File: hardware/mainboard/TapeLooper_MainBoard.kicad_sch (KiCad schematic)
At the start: 4 parts, among them J101 Micro_SD_Card, U101 DAISY_SEED

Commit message: hardware: resave files with KiCad v7.0.4
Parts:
- gave numbers to parts that had none: 2

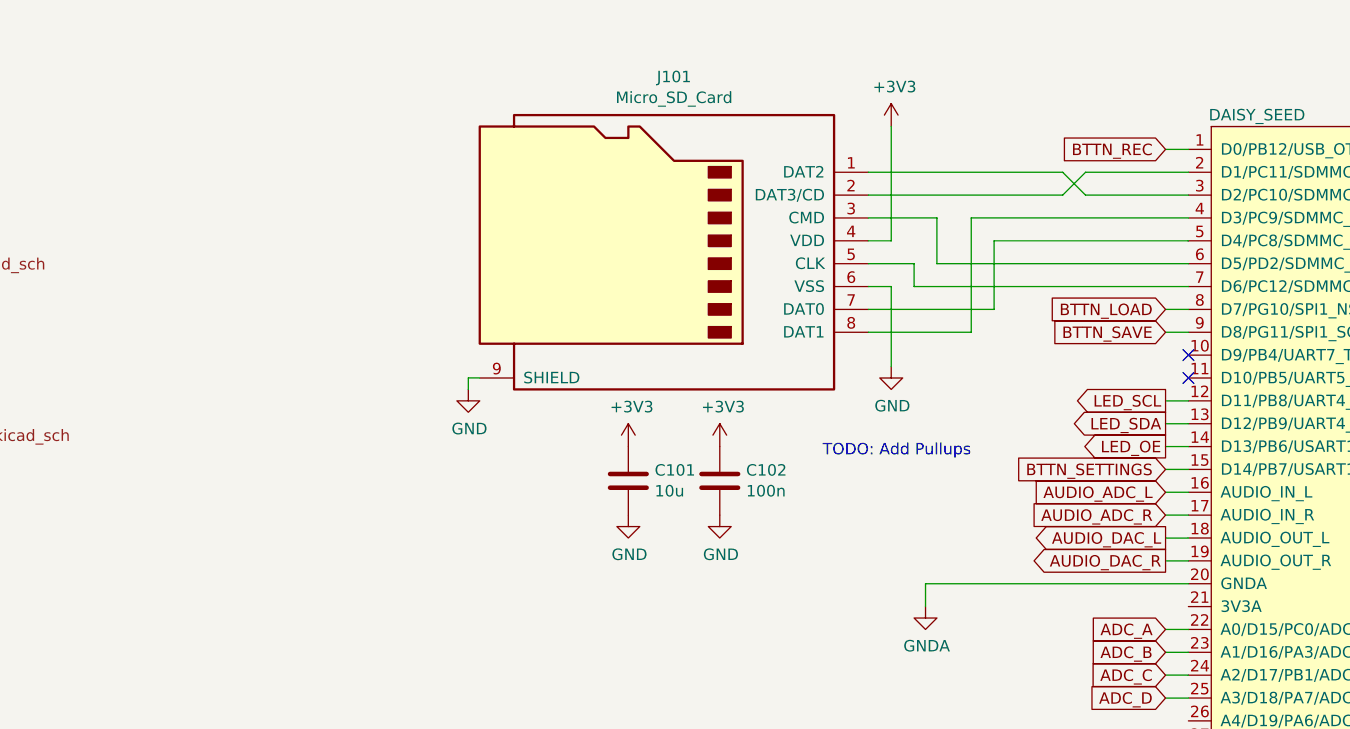
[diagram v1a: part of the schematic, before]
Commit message: hardware: add missing SD card pullups
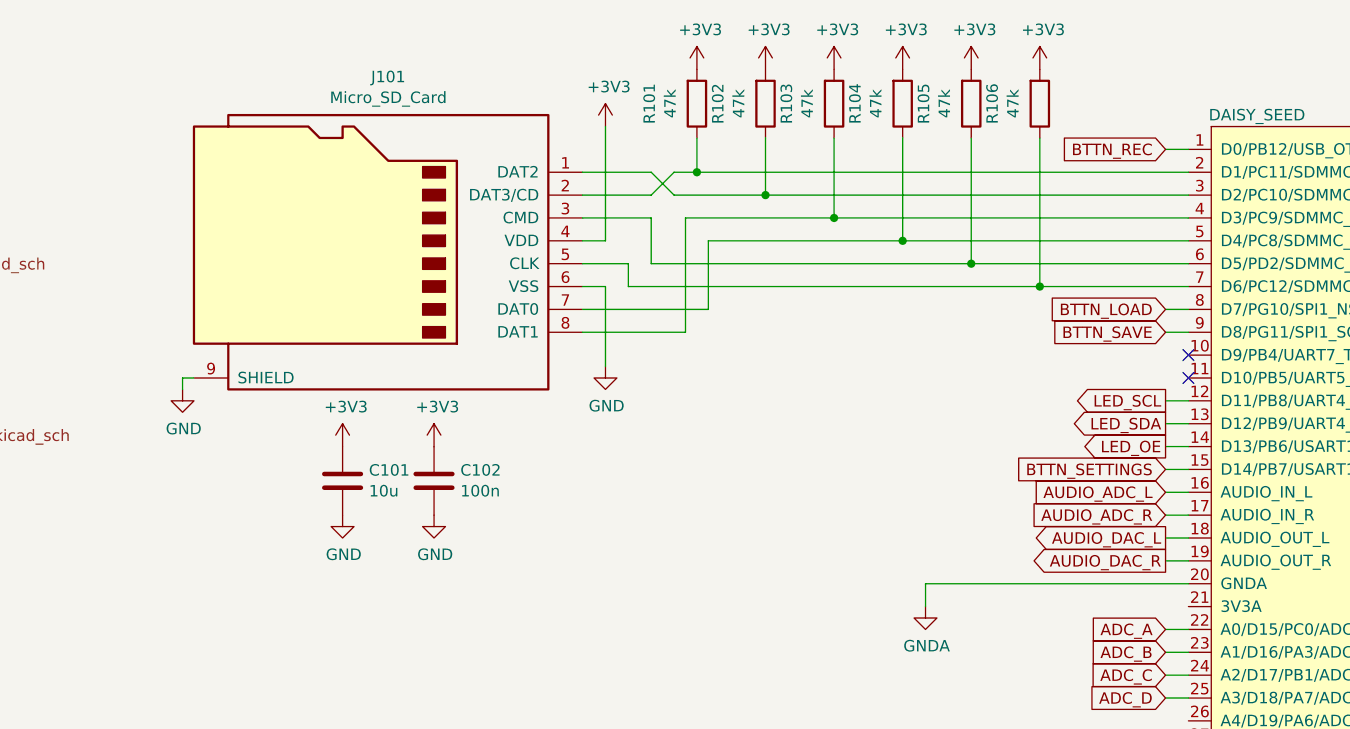
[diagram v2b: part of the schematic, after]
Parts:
- added R101, R102, R103, R104, R105, R106: 47k, Resistor_SMD:R_0603_1608Metric_Pad0.98x0.95mm_HandSolder, symbol Device:R
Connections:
- net +3V3: now also R101.2, R102.2, R103.2, R104.2, R105.2, R106.2
- net at J101.2 (DAT3/CD), U101.2 (D1/PC11/SDMMC_D3/UART3_RX/SPI3_MISO): now also R101.1
- net at J101.1 (DAT2), U101.3 (D2/PC10/SDMMC_D2/UART3_TX/SPI3_SCK): now also R102.1
- net at J101.8 (DAT1), U101.4 (D3/PC9/SDMMC_D1/I2C3_SDA/TIM3_4/TIM8_4): now also R103.1
- net at J101.7 (DAT0), U101.5 (D4/PC8/SDMMC_D0/HRTIM_B1/TIM3_3/TIM8_3): now also R104.1
- net at J101.3 (CMD), U101.6 (D5/PD2/SDMMC_CMD/UART5_RX): now also R105.1
- net at J101.5 (CLK), U101.7 (D6/PC12/SDMMC_CK/UART5_TX/SPI3_MOSI/I2S3_SDO/HTIM_EEV2): now also R106.1
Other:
- note removed: "TODO: Add Pullups"
- moved on the sheet: C101, C102, J101
